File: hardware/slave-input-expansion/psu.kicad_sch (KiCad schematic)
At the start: 15 parts, among them U8 AMS1117-5.0

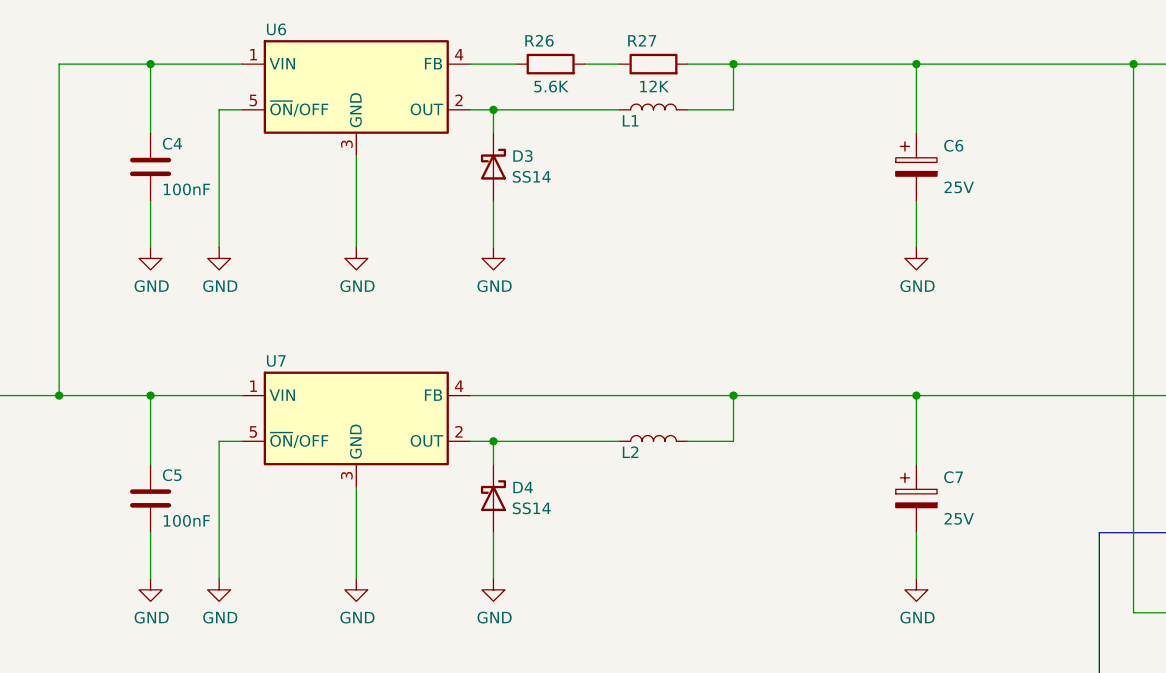
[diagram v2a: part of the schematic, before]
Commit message: switch to 12v psu
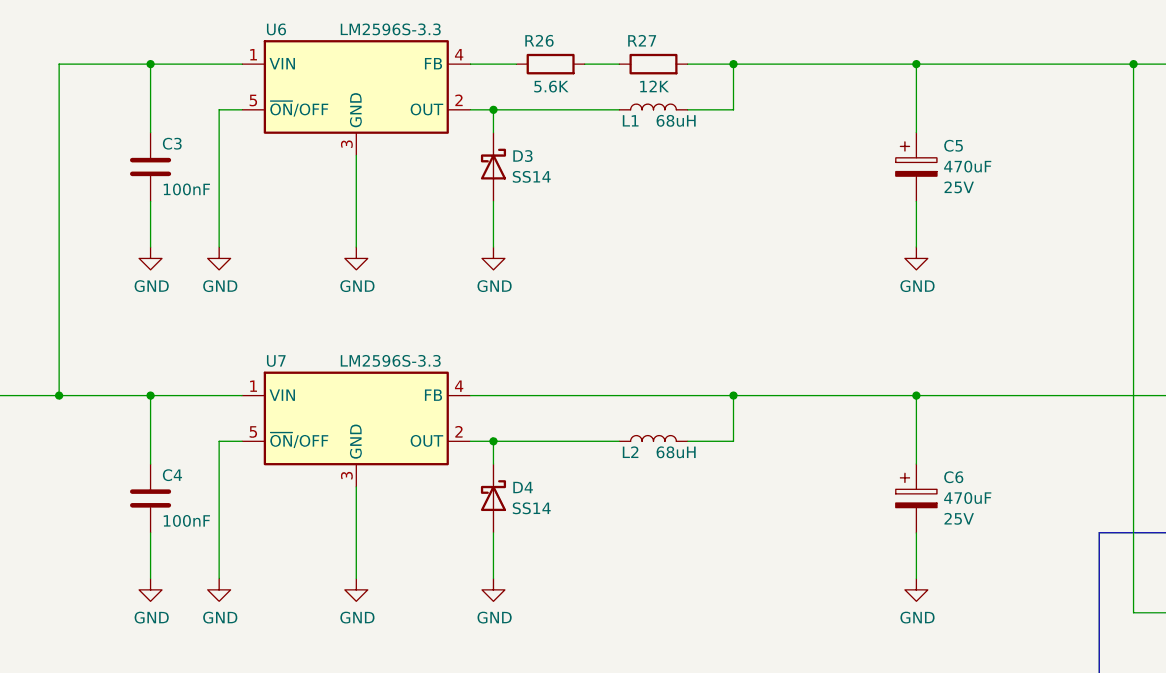
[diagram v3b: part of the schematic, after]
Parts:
- C5: renamed from C6; value (none) -> 470uF; footprint (none) -> Capacitor_SMD:CP_Elec_10x10
- C6: renamed from C7; value (none) -> 470uF; footprint (none) -> Capacitor_SMD:CP_Elec_10x10
- L1, L2: value (none) -> 68uH; footprint (none) -> Inductor_SMD:L_12x12mm_H8mm
- U6, U7: value (none) -> LM2596S-3.3; footprint (none) -> Package_TO_SOT_SMD:TO-263-5_TabPin3
- renumbered C4 to C3, C5 to C4
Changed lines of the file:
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@@
     (in_bom yes) (on_board yes)
     (property "Reference" "U7" (id 0) (at 107.95 80.01 0))
-    (property "Value" "" (id 1) (at 120.65 80.01 0))
-    (property "Footprint" "" (id 2) (at 118.11 92.71 0)
+    (property "Value" "LM2596S-3.3" (id 1) (at 120.65 80.01 0))
+    (property "Footprint" "Package_TO_SOT_SMD:TO-263-5_TabPin3" (id 2) (at 118.11 92.71 0)
       (effects (font (size 1.27 1.27) italic) (justify left) hide)
     )
@@
   (symbol (lib_id "Device:C") (at 93.98 95.25 0) (unit 1)
     (in_bom yes) (on_board yes)
-    (property "Reference" "C5" (id 0) (at 95.25 92.71 0)
+    (property "Reference" "C4" (id 0) (at 95.25 92.71 0)
       (effects (font (size 1.27 1.27)) (justify left))
     )
@@
   (symbol (lib_id "kicad-rescue:CP-Device") (at 179.07 95.25 0) (unit 1)
     (in_bom yes) (on_board yes)
-    (property "Reference" "C7" (id 0) (at 182.0672 92.9386 0)
-      (effects (font (size 1.27 1.27)) (justify left))
-    )
-    (property "Value" "" (id 1) (at 182.0672 95.25 0)
-      (effects (font (size 1.27 1.27)) (justify left))
-    )
-    (property "Footprint" "" (id 2) (at 180.0352 99.06 0)
+    (property "Reference" "C6" (id 0) (at 182.0672 92.9386 0)
+      (effects (font (size 1.27 1.27)) (justify left))
+    )
+    (property "Value" "470uF" (id 1) (at 182.0672 95.25 0)
+      (effects (font (size 1.27 1.27)) (justify left))
+    )
+    (property "Footprint" "Capacitor_SMD:CP_Elec_10x10" (id 2) (at 180.0352 99.06 0)
       (effects (font (size 1.27 1.27)) hide)
     )
@@
     (in_bom yes) (on_board yes)
     (property "Reference" "L2" (id 0) (at 147.32 90.17 90))
-    (property "Value" "" (id 1) (at 152.4 90.17 90))
-    (property "Footprint" "" (id 2) (at 149.86 88.9 0)
+    (property "Value" "68uH" (id 1) (at 152.4 90.17 90))
+    (property "Footprint" "Inductor_SMD:L_12x12mm_H8mm" (id 2) (at 149.86 88.9 0)
       (effects (font (size 1.27 1.27)) hide)
     )
@@
     (in_bom yes) (on_board yes)
     (property "Reference" "L1" (id 0) (at 147.32 53.34 90))
-    (property "Value" "" (id 1) (at 152.4 53.34 90))
-    (property "Footprint" "" (id 2) (at 149.86 52.07 0)
+    (property "Value" "68uH" (id 1) (at 152.4 53.34 90))
+    (property "Footprint" "Inductor_SMD:L_12x12mm_H8mm" (id 2) (at 149.86 52.07 0)
       (effects (font (size 1.27 1.27)) hide)
     )
@@
   (symbol (lib_id "kicad-rescue:CP-Device") (at 179.07 58.42 0) (unit 1)
     (in_bom yes) (on_board yes)
-    (property "Reference" "C6" (id 0) (at 182.0672 56.1086 0)
-      (effects (font (size 1.27 1.27)) (justify left))
-    )
-    (property "Value" "" (id 1) (at 182.0672 58.42 0)
-      (effects (font (size 1.27 1.27)) (justify left))
-    )
-    (property "Footprint" "" (id 2) (at 180.0352 62.23 0)
+    (property "Reference" "C5" (id 0) (at 182.0672 56.1086 0)
+      (effects (font (size 1.27 1.27)) (justify left))
+    )
+    (property "Value" "470uF" (id 1) (at 182.0672 58.42 0)
+      (effects (font (size 1.27 1.27)) (justify left))
+    )
+    (property "Footprint" "Capacitor_SMD:CP_Elec_10x10" (id 2) (at 180.0352 62.23 0)
       (effects (font (size 1.27 1.27)) hide)
     )
@@
     (in_bom yes) (on_board yes)
     (property "Reference" "U6" (id 0) (at 107.95 43.18 0))
-    (property "Value" "" (id 1) (at 120.65 43.18 0))
-    (property "Footprint" "" (id 2) (at 118.11 55.88 0)
+    (property "Value" "LM2596S-3.3" (id 1) (at 120.65 43.18 0))
+    (property "Footprint" "Package_TO_SOT_SMD:TO-263-5_TabPin3" (id 2) (at 118.11 55.88 0)
       (effects (font (size 1.27 1.27) italic) (justify left) hide)
     )
@@
   (symbol (lib_id "Device:C") (at 93.98 58.42 0) (unit 1)
     (in_bom yes) (on_board yes)
-    (property "Reference" "C4" (id 0) (at 95.25 55.88 0)
-      (effects (font (size 1.27 1.27)) (justify left))
-    )
+    (property "Reference" "C3" (id 0) (at 95.25 55.88 0)
+      (effects (font (size 1.27 1.27)) (justify left))
+    )
